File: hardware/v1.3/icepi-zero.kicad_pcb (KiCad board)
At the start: 4 copper layers, 65 x 30 mm, 165 parts, among them J1 Conn_02x20_Counter_Clockwise, J2 GPDI_C_1.3, J3 USB_C_Receptacle_USB2.0_14P, J4 USB_C_Receptacle_USB2.0_14P, J5 USB_C_Receptacle_USB2.0_14P, J6 Micro_SD_Card_Det2, SW1 SW_Push, SW2 SW_Push, U1 ECP5-CABGA256, U10 TPD2EUSB30A, U11 AS4C16M16SA, U12 W25Q128JVS, U2 TLV62569DBV, U3 TLV62569DBV, U4 TLV62569DBV, U5 TPD2EUSB30A, U6 PCA9306DC1, U7 TPD2EUSB30A, U8 TPD2EUSB30A, U9 FT231XQ, Y1 SG-8018CG 50.000000MHz

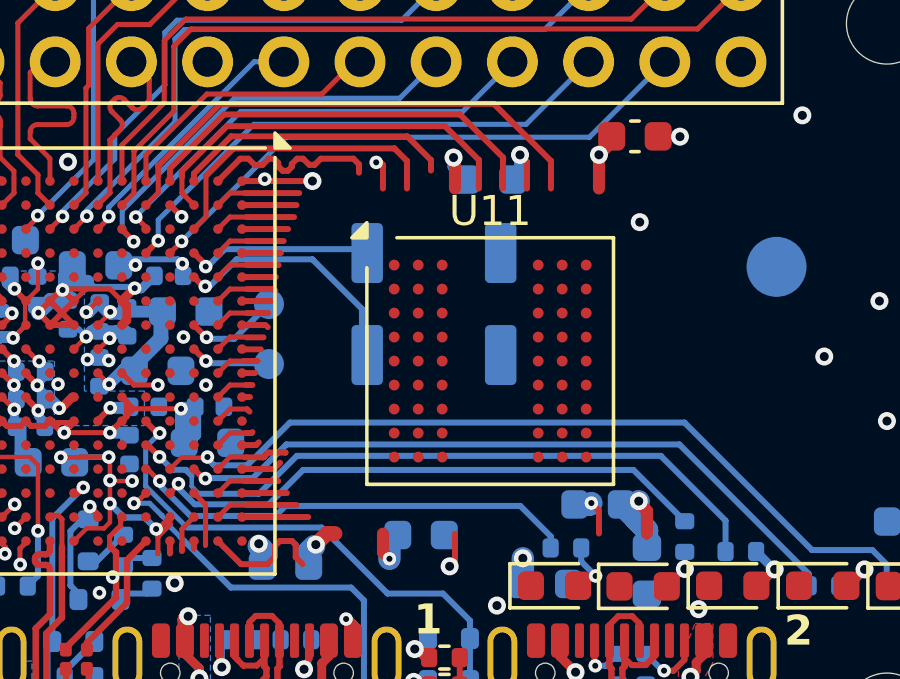
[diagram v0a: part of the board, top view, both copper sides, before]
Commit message: Replaced memory AS4C16M16SA 54-TFBGA (8x8)
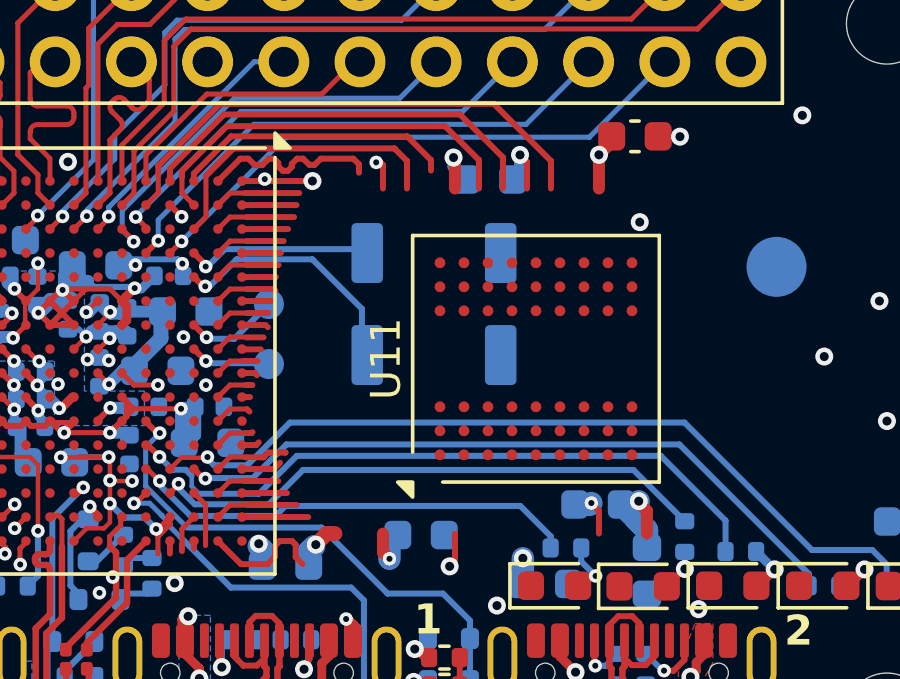
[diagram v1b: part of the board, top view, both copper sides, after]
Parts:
- moved U11 1.53 mm to (165.8, 104.7), turned to 90 degrees
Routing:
- net GND: track 106.3 -> 105.1 mm, vias 109 -> 108
- net /SDRAM/D2: track 0.25 -> 1.50 mm, vias 0 -> 1

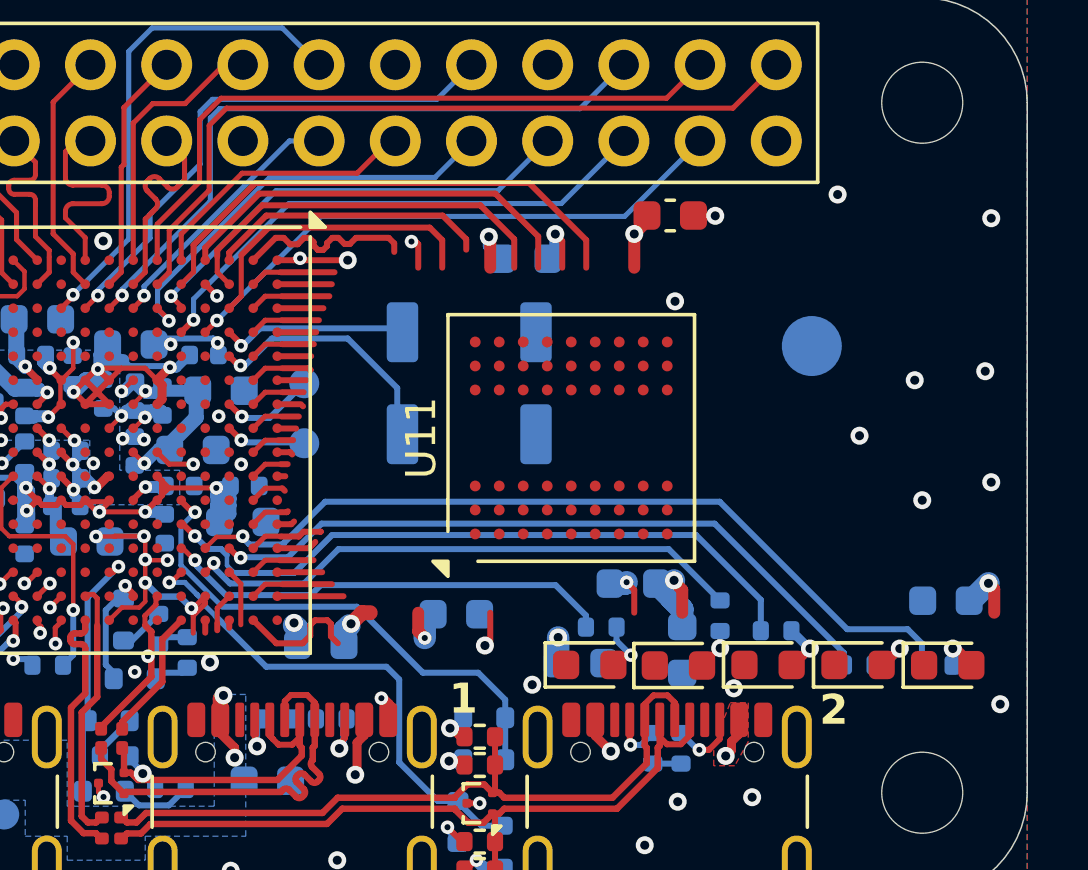
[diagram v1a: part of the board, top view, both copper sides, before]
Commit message: Removed LEDs D3, D4, D5
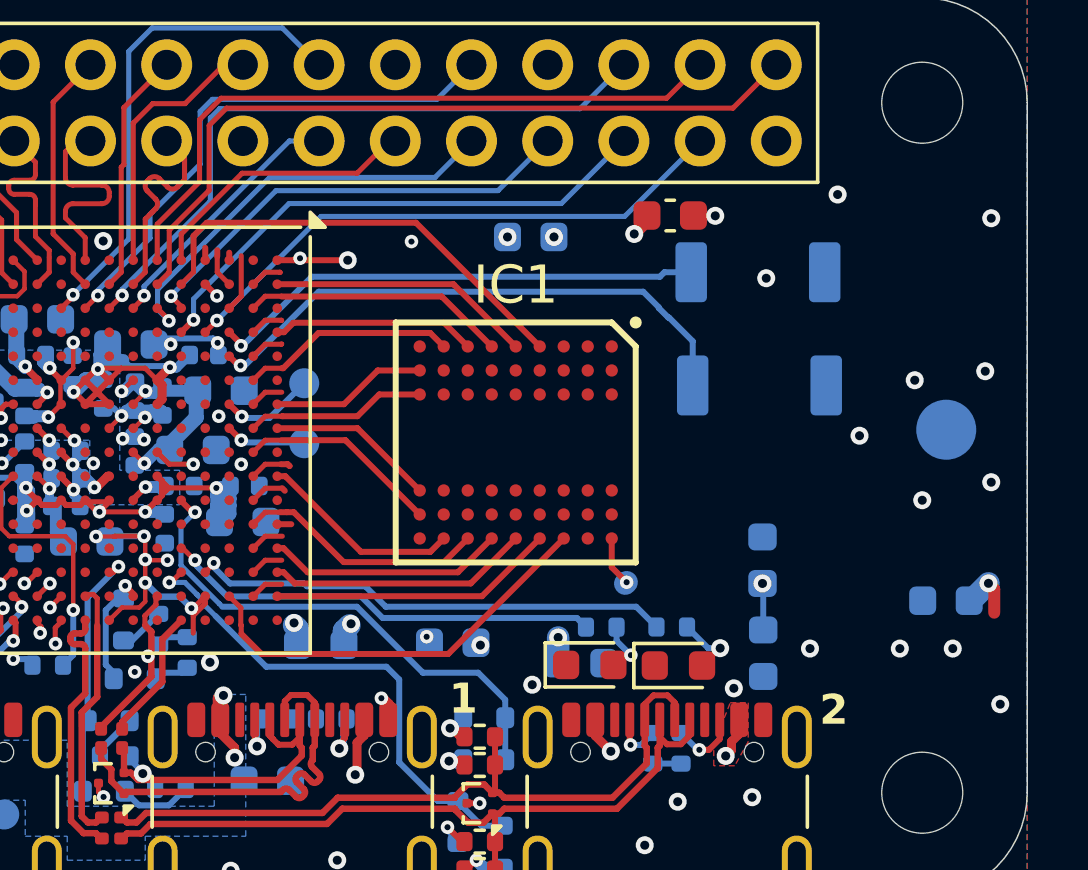
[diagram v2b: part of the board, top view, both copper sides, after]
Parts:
- removed D3, D4, D5: WHITE, LED_SMD:LED_0603_1608Metric
- removed R3, R4, R5: 470, Resistor_SMD:R_0402_1005Metric
- removed U11: AS4C16M16SA, Package_BGA:Alliance_TFBGA-54_8x8mm_Layout9x9_P0.8mm
- added IC1: IS42S16160J-6BLI, IS42S16160J-6BLI:BGA54C80P9X9_800X800X120, F.Cu at (163.9, 104.8)
- moved SW1 9.83 mm to (172.0, 99.2)
- moved SW2 9.81 mm to (172.1, 102.9)
- moved TP1 5.28 mm to (178.3, 104.4)
- moved C50 4.38 mm to (172.2, 108.8), turned to 90 degrees
- moved LOGO1 3.34 mm to (170.0, 106.1)
- moved C53 2.70 mm to (172.2, 111.8)
- moved R2 1.65 mm to (169.2, 111.0), turned to 0 degrees
- moved C47 0.96 mm to (161.8, 111.5)
- moved C52 0.75 mm to (164.4, 98.0)
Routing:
- net /LED4: track 27.5 -> 0.00 mm, vias 1 -> 0
- net /LED3: track 23.3 -> 0.00 mm, vias 1 -> 0
- net /LED2: track 22.6 -> 0.00 mm, vias 1 -> 0
- net /SDRAM/D11: track 13.9 -> 0.42 mm
- net /SDRAM/D3: track 1.30 -> 14.0 mm
- net /SDRAM/D12: track 13.3 -> 1.33 mm
- net /SW0: track 5.93 -> 16.6 mm
- net /SW1: track 8.23 -> 18.8 mm
- net /SDRAM/D13: track 9.34 -> 0.25 mm
- net /SDRAM/D14: track 10.1 -> 1.92 mm
- net /SDRAM/D5: track 2.21 -> 9.55 mm
- net /SDRAM/D7: track 1.50 -> 8.73 mm
- net /SDRAM/~{CS}: track 1.38 -> 8.38 mm
- net +3V3: track 94.9 -> 87.9 mm, vias 28 -> 29
- net /SDRAM/D8: track 1.82 -> 8.81 mm
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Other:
- board text added: "${REFERENCE}"

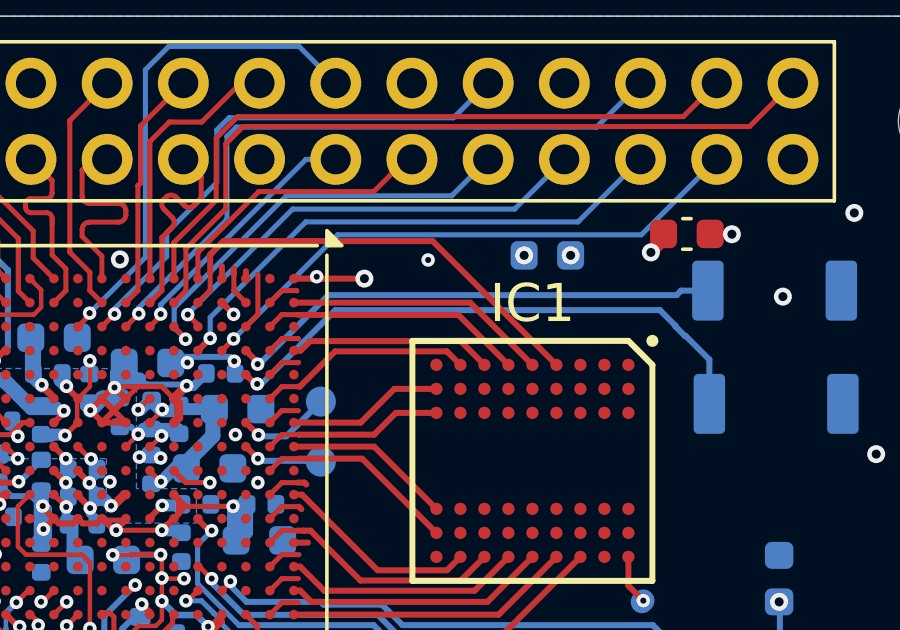
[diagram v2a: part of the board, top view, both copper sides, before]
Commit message: Added vias
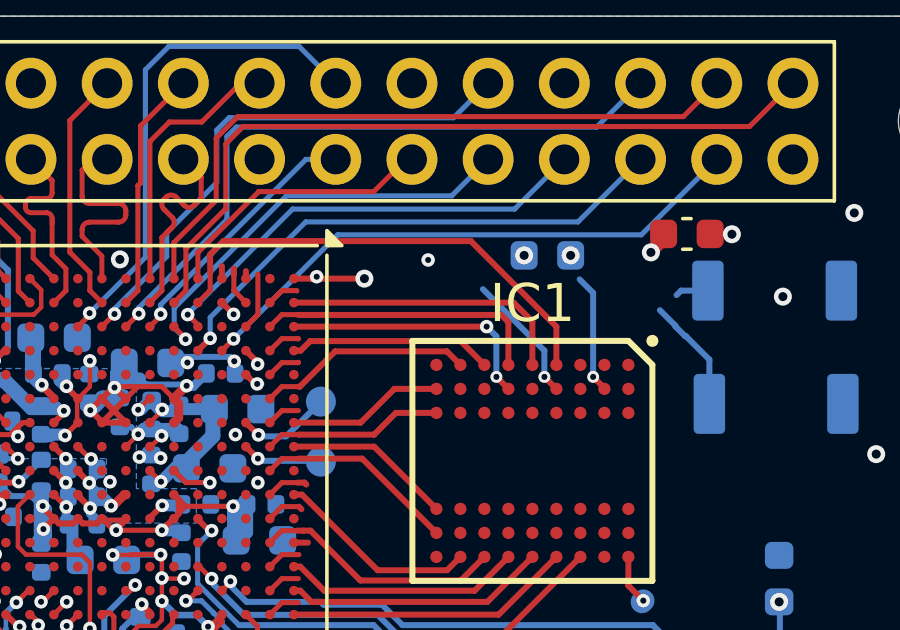
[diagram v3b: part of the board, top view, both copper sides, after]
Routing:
- net /SW0: track 16.6 -> 1.78 mm
- net /SW1: track 18.8 -> 4.52 mm
- net /SDRAM/CLK: track 0.00 -> 8.70 mm, vias 0 -> 2
- net /SDRAM/D9: track 1.07 -> 5.41 mm, vias 0 -> 1
- net /SDRAM/D13: track 0.25 -> 4.24 mm, vias 0 -> 1
- net /SDRAM/D8: track 8.81 -> 9.66 mm
- net /SDRAM/DQM1: track 8.81 -> 9.64 mm
- net /SDRAM/D10: track 15.2 -> 15.9 mm
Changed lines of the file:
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@@
 	)
 	(gr_text "${REFERENCE}"
-		(at 156.9 103.4 0)
+		(at 156.9 101.4 0)
 		(layer "B.Fab")
 		(effects
@@
 	)
 	(gr_text "${REFERENCE}"
-		(at 156.9 101.4 0)
+		(at 156.9 103.4 0)
 		(layer "B.Fab")
 		(effects
@@
 	)
 	(segment
-		(start 154.849432 101.600568)
-		(end 157.15 99.3)
-		(width 0.2)
-		(layer "B.Cu")
-		(net 115)
-	)
-	(segment
 		(start 168.90691 99.15)
 		(end 169.8 99.15)
@@
 	)
 	(segment
-		(start 157.15 99.3)
-		(end 168.75691 99.3)
-		(width 0.2)
-		(layer "B.Cu")
-		(net 115)
-	)
-	(segment
 		(start 154.776296 102.26)
 		(end 154.71 102.26)
@@
 	)
 	(segment
-		(start 157.38 99.8)
-		(end 168.2 99.8)
-		(width 0.2)
-		(layer "B.Cu")
-		(net 116)
-	)
-	(segment
-		(start 154.92 102.26)
-		(end 157.38 99.8)
-		(width 0.2)
-		(layer "B.Cu")
-		(net 116)
-	)
-	(segment
 		(start 154.4 104.35)
 		(end 154.8 104.75)
@@
 	)
 	(segment
-		(start 153.65 97.5)
-		(end 153.21 97.94)
-		(width 0.2)
-		(layer "F.Cu")
-		(net 124)
-	)
-	(segment
-		(start 160.625 97.5)
+		(start 161.9 97.5)
 		(end 153.65 97.5)
 		(width 0.2)
@@
 	)
 	(segment
-		(start 164.75 101.625)
-		(end 160.625 97.5)
-		(width 0.2)
-		(layer "F.Cu")
-		(net 124)
-	)
-	(segment
 		(start 152.8 99.55)
 		(end 153.21 99.14)
@@
 	)
 	(segment
-		(start 161.875 99.55)
-		(end 156 99.55)
+		(start 164.75 100.35)
+		(end 161.9 97.5)
+		(width 0.2)
+		(layer "F.Cu")
+		(net 124)
+	)
+	(segment
+		(start 164.75 101.625)
+		(end 164.75 100.35)
+		(width 0.2)
+		(layer "F.Cu")
+		(net 124)
+	)
+	(segment
+		(start 153.65 97.5)
+		(end 153.21 97.94)
+		(width 0.2)
+		(layer "F.Cu")
+		(net 124)
+	)
+	(segment
+		(start 163.95 100.175)
+		(end 163.325 99.55)
 		(width 0.2)
 		(layer "F.Cu")
@@
 	(segment
 		(start 163.95 101.625)
-		(end 161.875 99.55)
+		(end 163.95 100.175)
+		(width 0.2)
+		(layer "F.Cu")
+		(net 125)
+	)
+	(segment
+		(start 163.325 99.55)
+		(end 156 99.55)
 		(width 0.2)
 		(layer "F.Cu")
@@
 	)
 	(segment
+		(start 156 100.35)
+		(end 162.325 100.35)
+		(width 0.2)
+		(layer "F.Cu")
+		(net 137)
+	)
+	(segment
+		(start 162.75 102.025)
+		(end 163.15 102.425)
+		(width 0.2)
+		(layer "F.Cu")
+		(net 137)
+	)
+	(via
+		(at 162.425 100.35)
+		(size 0.45)
+		(drill 0.2)
+		(layers "F.Cu" "B.Cu")
+		(net 137)
+	)
+	(via
+		(at 162.75 102.025)
+		(size 0.4)
+		(drill 0.2)
+		(layers "F.Cu" "B.Cu")
+		(net 137)
+	)
+	(segment
+		(start 162.75 102.025)
+		(end 162.75 100.675)
+		(width 0.2)
+		(layer "B.Cu")
+		(net 137)
+	)
+	(segment
+		(start 162.75 100.675)
+		(end 162.425 100.35)
+		(width 0.2)
+		(layer "B.Cu")
+		(net 137)
+	)
+	(segment
 		(start 134.12 116.68)
 		(end 134.7425 116.68)
@@
 	)
 	(segment
+		(start 166.35 102.425)
+		(end 166.35 102.4)
+		(width 0.2)
+		(layer "F.Cu")
+		(net 173)
+	)
+	(segment
 		(start 154.4 98.497754)
 		(end 154.4 98.75)
@@
 	)
 	(segment
+		(start 166.35 102.4)
+		(end 165.975 102.025)
+		(width 0.2)
+		(layer "F.Cu")
+		(net 173)
+	)
+	(via
+		(at 165.975 102.025)
+		(size 0.4)
+		(drill 0.2)
+		(layers "F.Cu" "B.Cu")
+		(free yes)
+		(net 173)
+	)
+	(segment
+		(start 165.975 99.225)
+		(end 165.525 98.775)
+		(width 0.2)
+		(layer "B.Cu")
+		(net 173)
+	)
+	(segment
+		(start 165.975 102.025)
+		(end 165.975 99.225)
+		(width 0.2)
+		(layer "B.Cu")
+		(net 173)
+	)
+	(segment
 		(start 147.576 99.126)
 		(end 147.2 98.75)
@@
 	)
 	(segment
+		(start 164.35 102.025)
+		(end 164.75 102.425)
+		(width 0.2)
+		(layer "F.Cu")
+		(net 210)
+	)
+	(segment
 		(start 155.6 99.15)
 		(end 156.09 99.15)
@@
 		(net 210)
 	)
+	(via
+		(at 164.35 102.025)
+		(size 0.4)
+		(drill 0.2)
+		(layers "F.Cu" "B.Cu")
+		(free yes)
+		(net 210)
+	)
+	(segment
+		(start 164.35 102.025)
+		(end 164.35 101.15)
+		(width 0.2)
+		(layer "B.Cu")
+		(net 210)
+	)
+	(segment
+		(start 164.35 101.15)
+		(end 162.3 99.1)
+		(width 0.2)
+		(layer "B.Cu")
+		(net 210)
+	)
 	(segment
 		(start 155.2 106.75)
@@
 	)
 	(segment
-		(start 161.485 99.96)
-		(end 156.15 99.96)
-		(width 0.2)
+		(start 155.2 100.35)
+		(end 155.6 99.95)
+		(width 0.17)
 		(layer "F.Cu")
 		(net 249)
 	)
 	(segment
-		(start 155.2 100.35)
-		(end 155.6 99.95)
-		(width 0.17)
+		(start 163.15 101.625)
+		(end 163.15 100.2)
+		(width 0.2)
 		(layer "F.Cu")
 		(net 249)
@@
 	)
 	(segment
-		(start 163.15 101.625)
-		(end 161.485 99.96)
+		(start 162.91 99.96)
+		(end 156.15 99.96)
 		(width 0.2)
 		(layer "F.Cu")
@@
 		(layer "F.Cu")
 		(net 249)
+	)
+	(segment
+		(start 163.15 100.2)
+		(end 162.91 99.96)
+		(width 0.2)
+		(layer "F.Cu")
+		(net 249)

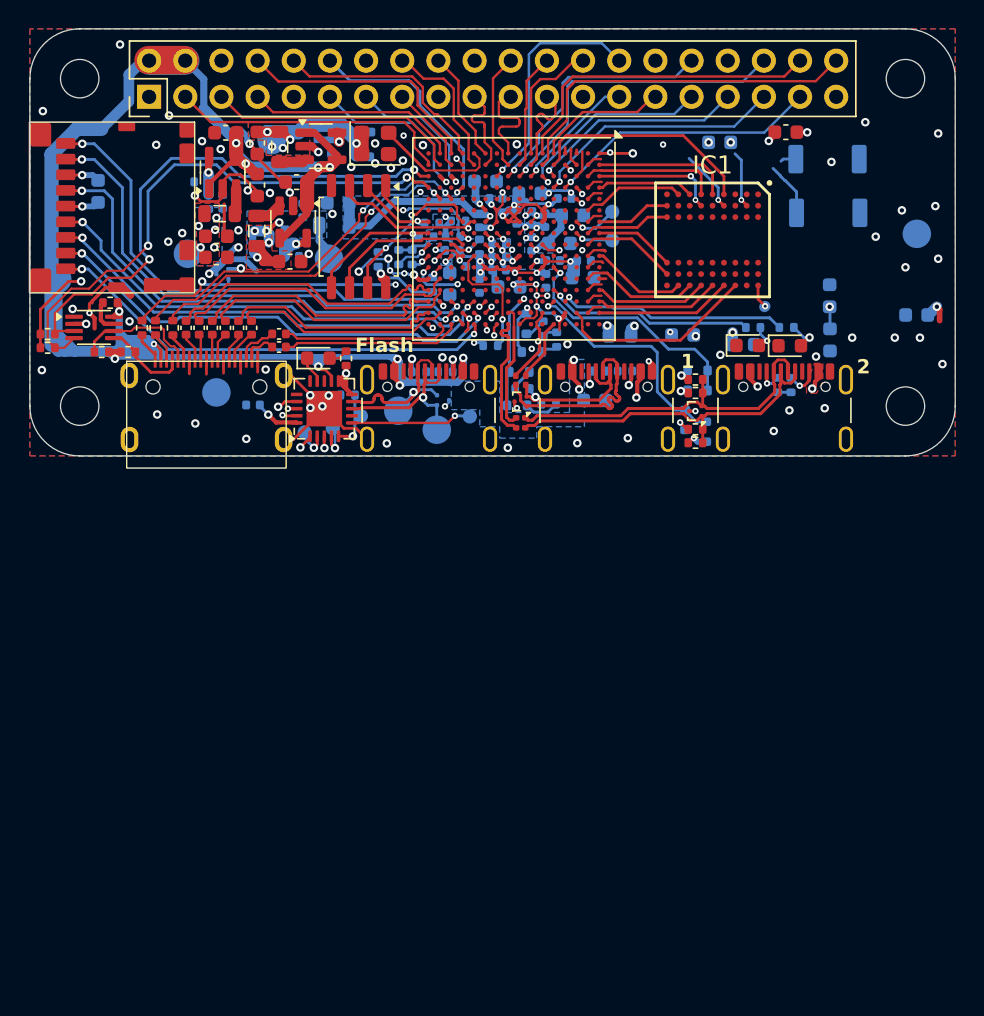
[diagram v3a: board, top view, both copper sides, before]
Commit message: Connected traces to memory
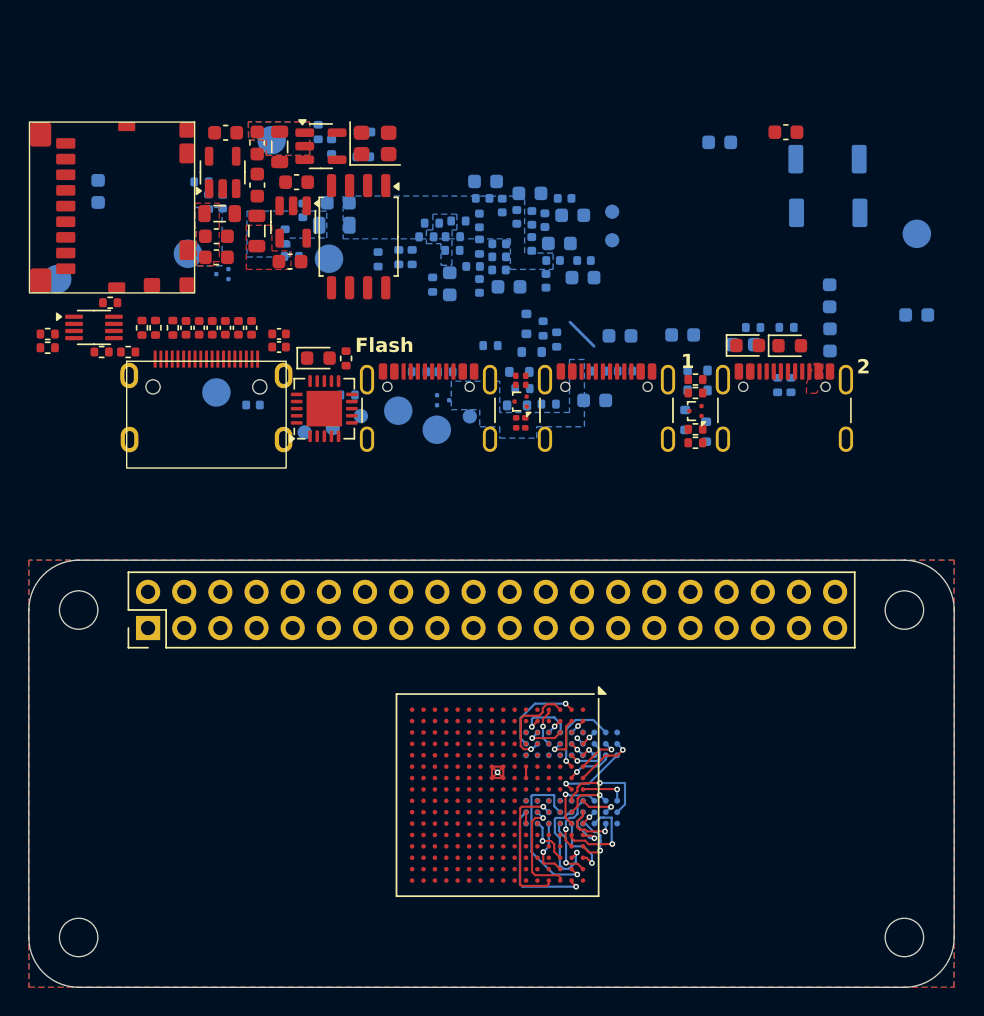
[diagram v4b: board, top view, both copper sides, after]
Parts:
- IC1: moved to B.Cu
- moved U1 39.1 mm to (148.8, 143.8)
- moved IC1 39.1 mm to (154.1, 142.6)
- moved H1 37.3 mm to (119.4, 130.8)
- moved H2 37.3 mm to (177.4, 130.8)
- moved H3 37.3 mm to (119.4, 153.8)
- moved H4 37.3 mm to (177.4, 153.8)
- moved J1 37.3 mm to (124.3, 132.1)
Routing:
- net +5V: track 196.1 -> 49.1 mm, vias 16 -> 0
- net GND: track 100.6 -> 2.13 mm, vias 108 -> 0
- net +3V3: track 87.9 -> 7.76 mm, vias 29 -> 1
- net /GPDI/GPDI_SDA_3V3: track 38.6 -> 0.00 mm, vias 2 -> 0
- net /GPDI/GPDI_SCK_3V3: track 38.3 -> 0.00 mm, vias 2 -> 0
- net /uSD/SD_DAT0: track 35.3 -> 0.00 mm, vias 2 -> 0
- net /uSD/SD_DAT1: track 34.6 -> 0.00 mm, vias 2 -> 0
- net /uSD/SD_CLK: track 33.2 -> 0.00 mm, vias 2 -> 0
- net /uSD/SD_DAT2: track 33.0 -> 0.00 mm, vias 2 -> 0
- net /uSD/SD_DAT3: track 32.9 -> 0.00 mm, vias 2 -> 0
- net /uSD/SD_DET: track 32.2 -> 0.00 mm, vias 2 -> 0
- net /uSD/SD_CMD: track 31.7 -> 0.00 mm, vias 2 -> 0
- net /GPDI/GPDI_UTIL: track 26.4 -> 0.00 mm, vias 3 -> 0
- net /GPIO21: track 25.8 -> 0.00 mm
- net /USB/D1I+: track 25.1 -> 0.00 mm
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
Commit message: Update icepi-zero.kicad_pcb
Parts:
- moved C15 45.4 mm to (147.3, 146.6)
- moved FB1 41.9 mm to (145.8, 144.8)
- moved C17 41.3 mm to (148.2, 144.8), turned to 90 degrees
- moved C16 37.3 mm to (147.8, 143.2)
- moved C2 34.5 mm to (145.5, 142.3), turned to 90 degrees
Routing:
- net /Power/FILTERED_2V5: track 0.00 -> 13.9 mm, vias 0 -> 5
- net GND: track 2.13 -> 15.9 mm, vias 0 -> 1
- net +1V1: track 24.7 -> 35.0 mm, vias 0 -> 3

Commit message: Update icepi-zero.kicad_pcb
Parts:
- moved C4 43.1 mm to (152.1, 146.1), turned to -90 degrees
- moved C6 42.3 mm to (149.9, 145.6)
- moved C10 40.5 mm to (148.9, 145.6), turned to -90 degrees
- moved C5 40.0 mm to (151.6, 143.5), turned to 90 degrees
- moved C8 38.7 mm to (150.9, 145.6), turned to -90 degrees
- moved C7 38.4 mm to (150.6, 143.5)
- moved C3 37.8 mm to (152.9, 142.9), turned to 90 degrees
- moved C9 37.5 mm to (149.5, 143.5), turned to 90 degrees
- moved FB1 9.04 mm to (154.8, 145.5)
- moved C2 9.02 mm to (154.5, 142.9)
- moved C15 8.88 mm to (156.1, 147.3)
- moved U1 8.88 mm to (157.7, 144.5)
- moved C16 8.88 mm to (156.7, 143.8)
- moved C17 8.88 mm to (157.1, 145.4)
- moved IC1 8.88 mm to (162.9, 143.3)
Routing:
- net +1V1: track 35.0 -> 44.8 mm
- net GND: track 15.9 -> 25.5 mm
- net /SDRAM/D13: track 6.85 -> 0.61 mm
- net /GPIO15: track 0.00 -> 2.91 mm
- net /SDRAM/D9: track 3.46 -> 0.55 mm
- net /SDRAM/A2: track 6.86 -> 4.05 mm
- net /Flash/~{FLASH_CS}: track 0.00 -> 2.81 mm
- net /SDRAM/BA1: track 4.44 -> 2.21 mm
- net /GPIO22: track 0.00 -> 2.13 mm
- net /SDRAM/D14: track 2.68 -> 0.55 mm
- net /uSD/SD_DAT0: track 0.00 -> 2.12 mm
- net /SDRAM/D3: track 4.29 -> 2.17 mm
- net unconnected-(U1E-PR44D/-/RSQ44-PadN12): track 0.00 -> 1.39 mm
- net /SDRAM/~{CAS}: track 4.05 -> 2.66 mm
- net /Power/FILTERED_2V5: track 13.9 -> 12.6 mm
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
